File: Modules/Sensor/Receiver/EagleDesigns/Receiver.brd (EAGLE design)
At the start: 100 x 80 mm, 11 parts, among them U2 ATMEGA328P_TQFP

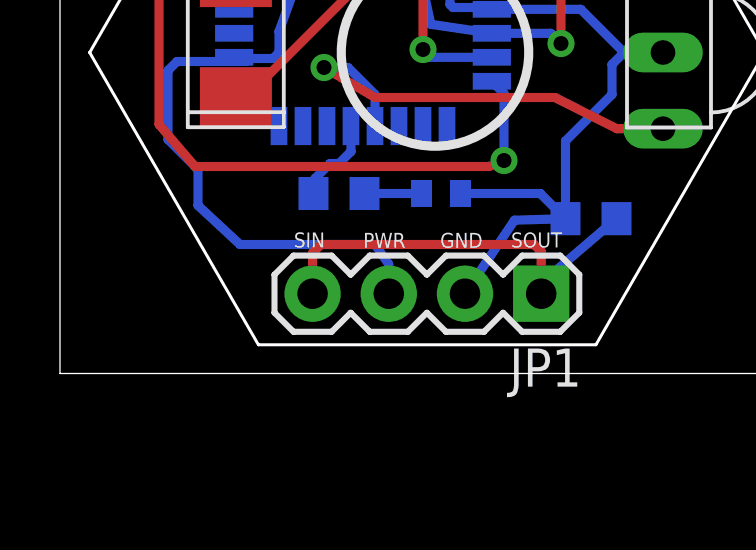
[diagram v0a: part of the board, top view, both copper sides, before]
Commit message: fixed eagle files for new modules
SIN/SOUT was not correctly connected in them.
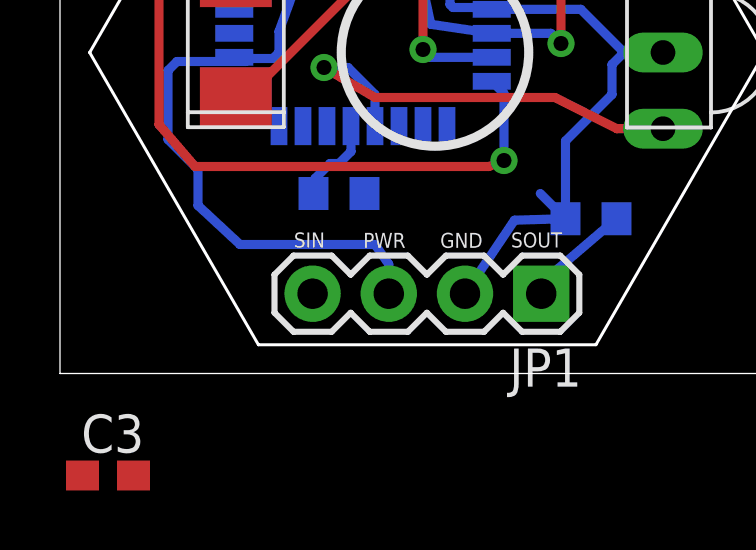
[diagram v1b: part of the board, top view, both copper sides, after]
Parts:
- C3: device adafruit:C0402 -> adafruit:C0603
- moved C3 14.5 mm to (1.60, -3.40), flipped to the top, turned to 0 degrees
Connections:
- removed net 1X3SIN-SOUT: JP1.1, JP1.4, R1.2
- net 1X3SIN: now also JP1.4, R1.2
- net 1X3SOUT: now also JP1.1
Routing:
- net 1X3SIN-SOUT: track 14.4 -> 0.00 mm
- net 1X3SIN: track 0.00 -> 3.55 mm
- net GND: track 43.7 -> 41.0 mm
- net 1X3SOUT: track 1.90 -> 0.00 mm
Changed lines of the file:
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@@
 </element>
 <element name="R4" library="adafruit" package="R0603" value="4.7K" x="9.3" y="6" rot="MR0"/>
-<element name="C3" library="adafruit" package="C0402" value="0.22uF" x="12.7" y="6" rot="MR180"/>
 <element name="U$1" library="tsop" package="TSOP382XX,384XX" value="TSOP38238" x="21.7" y="10.7" rot="R90"/>
+<element name="C3" library="adafruit" package="C0603" value="0.22uF" x="1.6" y="-3.4"/>
 </elements>
 <signals>
@@
 <wire x1="16.85" y1="5.16" x2="15.15" y2="5.11" width="0.3048" layer="16"/>
 <wire x1="15.15" y1="5.11" x2="13.5" y2="2.66" width="0.3048" layer="16"/>
-<contactref element="C3" pad="2"/>
 <contactref element="U$1" pad="GND"/>
 <wire x1="12.25" y1="16.55" x2="9.95" y2="16.55" width="0.3048" layer="1"/>
@@
 <wire x1="14.3926" y1="12.14" x2="17.36" y2="12.14" width="0.3048" layer="16"/>
 <wire x1="17.36" y1="12.14" x2="18.8" y2="10.7" width="0.3048" layer="16"/>
-<wire x1="13.35" y1="6" x2="16.01" y2="6" width="0.3048" layer="16"/>
 <wire x1="16.01" y1="6" x2="16.85" y2="5.16" width="0.3048" layer="16"/>
 <wire x1="7.89" y1="16.55" x2="9.95" y2="16.55" width="0.3048" layer="1"/>
@@
 <via x="10" y="14.7" extent="1-16" drill="0.5"/>
 <wire x1="10" y1="14.7" x2="10" y2="15.5" width="0.3048" layer="16"/>
-</signal>
-<signal name="1X3SIN-SOUT">
-<contactref element="JP1" pad="4"/>
-<contactref element="JP1" pad="1"/>
-<contactref element="R1" pad="2"/>
-<wire x1="18.55" y1="5.16" x2="15.85" y2="2.85" width="0.3048" layer="16"/>
-<wire x1="15.85" y1="2.85" x2="16.04" y2="2.66" width="0.3048" layer="16"/>
-<wire x1="16.04" y1="2.66" x2="16.04" y2="4.06" width="0.3048" layer="1"/>
-<wire x1="16.04" y1="4.06" x2="15.8" y2="4.3" width="0.3048" layer="1"/>
-<wire x1="8.42" y1="2.66" x2="8.42" y2="4.02" width="0.3048" layer="1"/>
-<wire x1="8.42" y1="4.02" x2="8.7" y2="4.3" width="0.3048" layer="1"/>
-<wire x1="8.7" y1="4.3" x2="15.8" y2="4.3" width="0.3048" layer="1"/>
+<contactref element="C3" pad="2"/>
+<wire x1="2.45" y1="-3.4" x2="13.5" y2="2.66" width="0" layer="19" extent="1-1"/>
 </signal>
 <signal name="RESET">
@@
 <signal name="1X3SIN">
 <contactref element="U2" pad="23"/>
+<contactref element="JP1" pad="4"/>
+<contactref element="R1" pad="2"/>
+<wire x1="18.55" y1="5.16" x2="15.85" y2="2.85" width="0.3048" layer="16"/>
+<wire x1="8.42" y1="2.66" x2="5.8074" y2="14.54" width="0" layer="19" extent="16-16"/>
+<wire x1="15.85" y1="2.85" x2="8.42" y2="2.66" width="0" layer="19" extent="16-16"/>
 </signal>
 <signal name="N$1">
@@
 <contactref element="R4" pad="1"/>
 <contactref element="C3" pad="1"/>
-<wire x1="10.15" y1="6" x2="12.05" y2="6" width="0.3048" layer="16"/>
+<contactref element="JP1" pad="1"/>
+<wire x1="10.15" y1="6" x2="16.04" y2="2.66" width="0" layer="19" extent="16-16"/>
+<wire x1="0.75" y1="-3.4" x2="10.15" y2="6" width="0" layer="19" extent="1-16"/>
 </signal>
 <signal name="OUT">

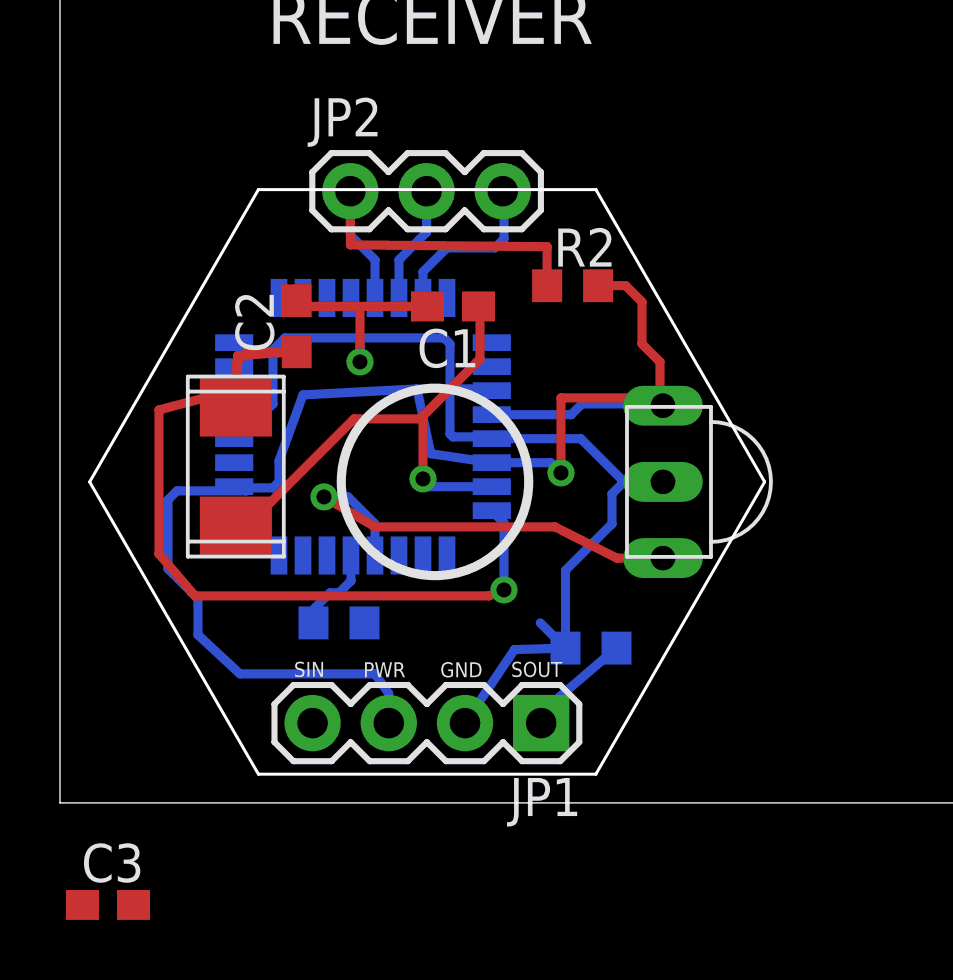
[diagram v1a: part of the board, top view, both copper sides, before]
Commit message: Receiver: added final PCB #29
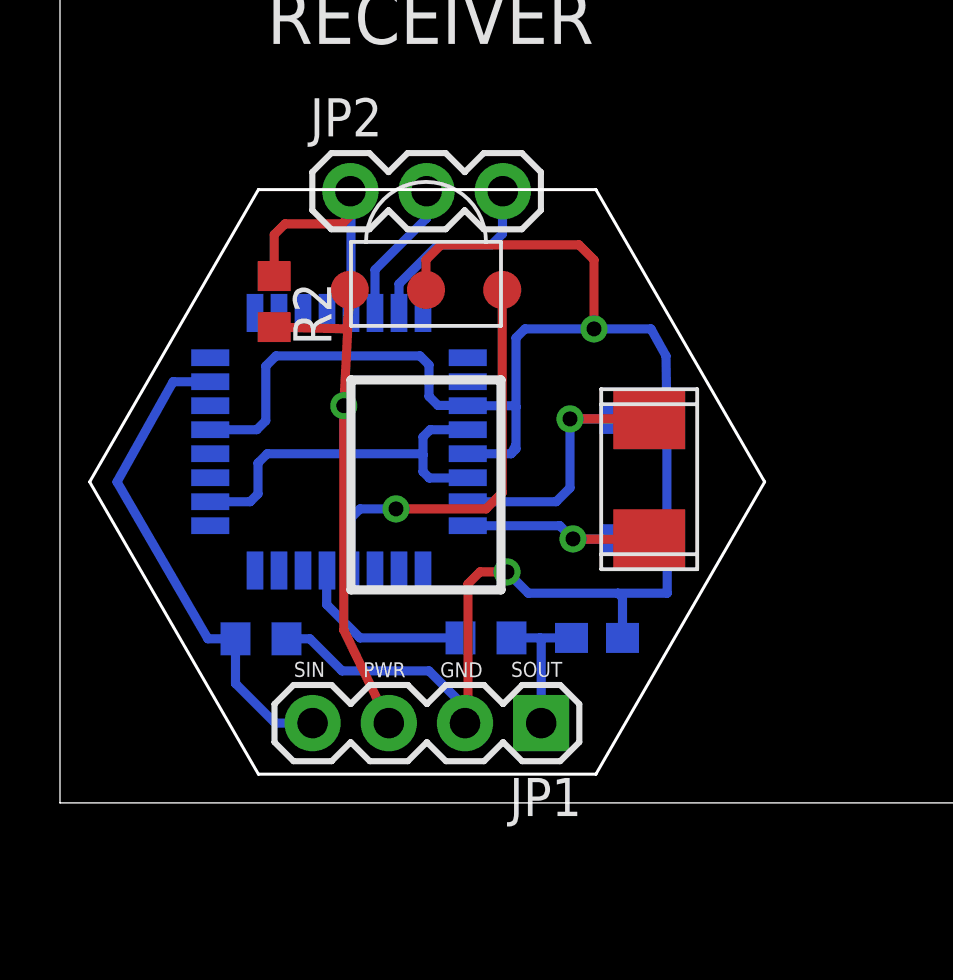
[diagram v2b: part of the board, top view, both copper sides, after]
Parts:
- U$1: value TSOP38238 -> IR-RECEIVER; device tsop:TSOP382XX,384XX -> MakerWear:TSOP382XX,384XX
- moved C3 18.6 mm to (17.9, 5.50), flipped to the bottom, turned to 180 degrees
- moved U$2 13.8 mm to (19.6, 10.8), turned to 270 degrees
- moved C2 13.5 mm to (19.4, 8.79), flipped to the bottom, turned to 180 degrees
- moved U$1 12.4 mm to (12.2, 18.7), turned to 180 degrees
- moved R1 11.0 mm to (6.70, 5.47), turned to 0 degrees
- moved R2 9.96 mm to (7.14, 16.7), turned to 270 degrees
- moved C1 7.31 mm to (19.4, 12.8), flipped to the bottom
- moved R4 4.93 mm to (14.2, 5.50)
- moved U2 0.94 mm to (9.30, 12.0)
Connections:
- net VCC: now also U$1.VSS; no longer U$1.VS
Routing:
- net GND: track 41.0 -> 62.9 mm, vias 1 -> 2
- net N$3: track 29.2 -> 7.68 mm
- net VCC: track 48.4 -> 32.9 mm
- net 1X3SIN: track 3.55 -> 16.6 mm
- net N$1: track 17.7 -> 10.1 mm
- net 1X3SOUT: track 0.00 -> 4.86 mm
- net RESET: track 13.5 -> 9.08 mm
- net OUT: track 2.94 -> 6.06 mm
- net IR-IN: track 14.9 -> 13.9 mm
- net TX: track 5.62 -> 6.53 mm
- net RX: track 3.94 -> 4.77 mm

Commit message: minor organizations
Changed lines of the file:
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@@
 <wire x1="9.5" y1="11.64" x2="12.06" y2="11.64" width="0.3048" layer="16"/>
 <wire x1="12.06" y1="11.64" x2="12.1" y2="11.6" width="0.3048" layer="16"/>
-<wire x1="9.66" y1="17.1" x2="9.46" y2="13.24" width="0.3048" layer="1"/>
-<via x="9.46" y="13.24" extent="1-16" drill="0.5"/>
-<wire x1="10.96" y1="2.66" x2="9.46" y2="5.76" width="0.3048" layer="1"/>
-<wire x1="9.46" y1="5.76" x2="9.46" y2="13.24" width="0.3048" layer="1"/>
-<wire x1="9.46" y1="13.24" x2="9.46" y2="11.68" width="0.3048" layer="16"/>
-<wire x1="9.46" y1="11.68" x2="9.5" y2="11.64" width="0.3048" layer="16"/>
-<wire x1="9.66" y1="17.1" x2="9.58" y2="15.8" width="0.3048" layer="1"/>
-<wire x1="9.58" y1="15.8" x2="7.14" y2="15.86" width="0.3048" layer="1"/>
+<via x="9.66" y="13.24" extent="1-16" drill="0.5"/>
+<wire x1="9.66" y1="13.24" x2="9.66" y2="11.68" width="0.3048" layer="16"/>
+<wire x1="9.66" y1="11.68" x2="9.5" y2="11.64" width="0.3048" layer="16"/>
+<wire x1="7.14" y1="15.86" x2="9.66" y2="15.86" width="0.3048" layer="1"/>
+<wire x1="9.66" y1="15.86" x2="9.66" y2="17.1" width="0.3048" layer="1"/>
+<wire x1="9.66" y1="15.86" x2="9.66" y2="13.24" width="0.3048" layer="1"/>
+<wire x1="9.66" y1="5.34" x2="9.66" y2="13.24" width="0.3048" layer="1"/>
+<wire x1="10.96" y1="2.66" x2="10.96" y2="4.84" width="0.3048" layer="1"/>
+<wire x1="10.96" y1="4.84" x2="10.7" y2="5.1" width="0.3048" layer="1"/>
+<wire x1="9.66" y1="5.34" x2="9.9" y2="5.1" width="0.3048" layer="1"/>
+<wire x1="9.9" y1="5.1" x2="10.7" y2="5.1" width="0.3048" layer="1"/>
 </signal>
 <signal name="GND">

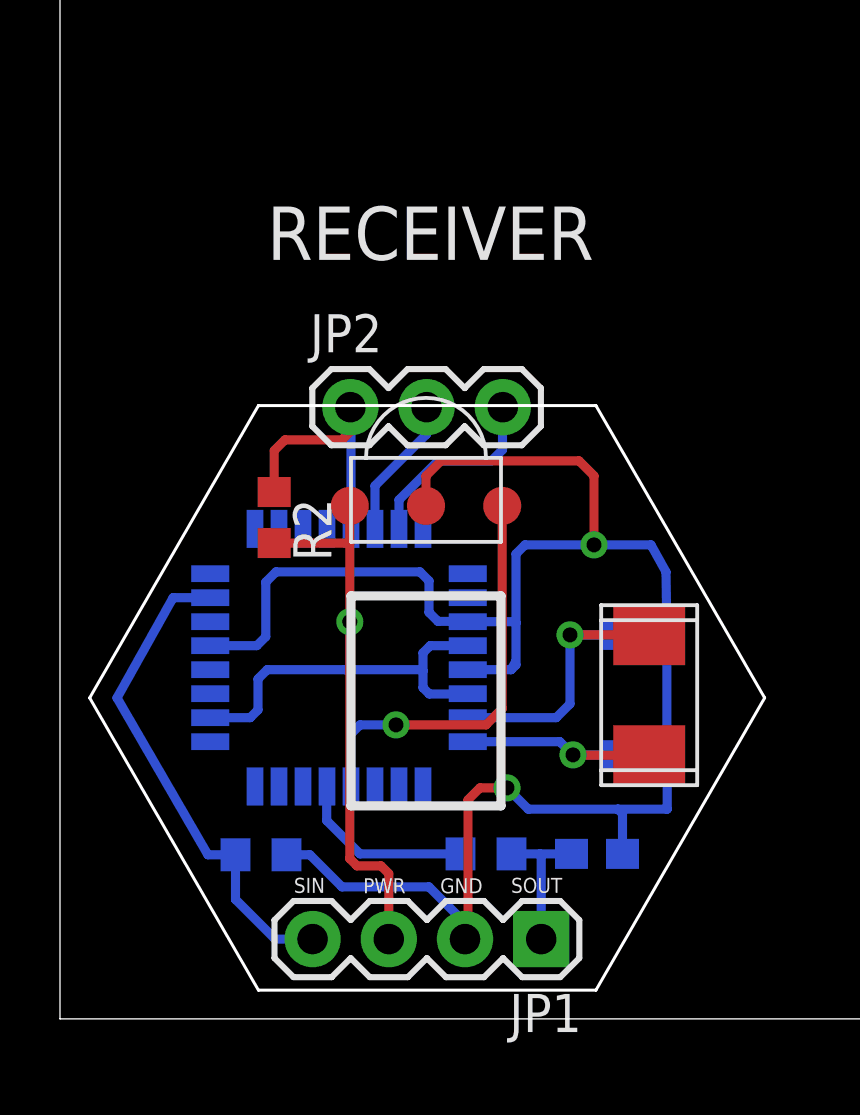
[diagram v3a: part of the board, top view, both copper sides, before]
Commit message: added version numbers, and deleted most of the text that was on each module.
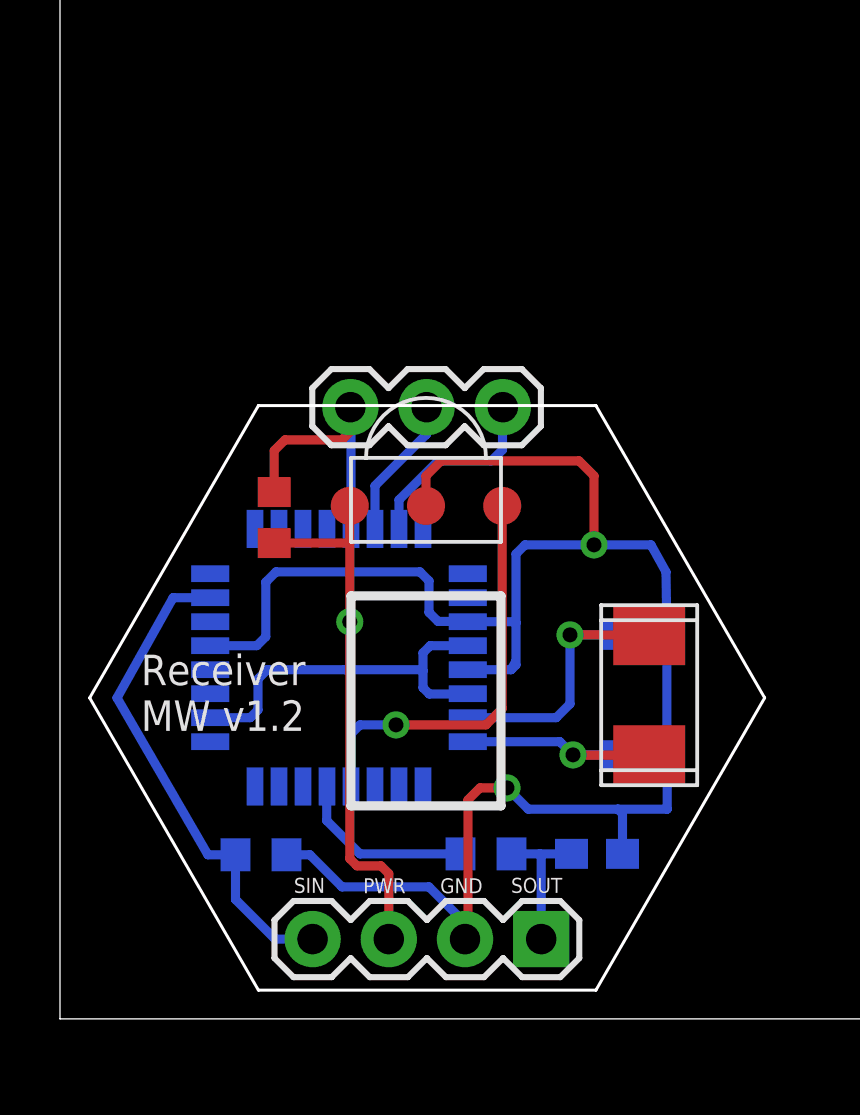
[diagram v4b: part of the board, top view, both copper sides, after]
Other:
- board text added: "Receiver MW v1.2"
- board text removed: "RECEIVER"
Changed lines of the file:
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@@
 <layer number="19" name="Unrouted" color="6" fill="1" visible="yes" active="yes"/>
 <layer number="20" name="Dimension" color="15" fill="1" visible="yes" active="yes"/>
-<layer number="21" name="tPlace" color="7" fill="1" visible="no" active="yes"/>
-<layer number="22" name="bPlace" color="7" fill="1" visible="no" active="yes"/>
-<layer number="23" name="tOrigins" color="15" fill="1" visible="no" active="yes"/>
-<layer number="24" name="bOrigins" color="15" fill="1" visible="no" active="yes"/>
-<layer number="25" name="tNames" color="7" fill="1" visible="no" active="yes"/>
-<layer number="26" name="bNames" color="7" fill="1" visible="no" active="yes"/>
-<layer number="27" name="tValues" color="7" fill="1" visible="no" active="yes"/>
-<layer number="28" name="bValues" color="7" fill="1" visible="no" active="yes"/>
+<layer number="21" name="tPlace" color="7" fill="1" visible="yes" active="yes"/>
+<layer number="22" name="bPlace" color="7" fill="1" visible="yes" active="yes"/>
+<layer number="23" name="tOrigins" color="15" fill="1" visible="yes" active="yes"/>
+<layer number="24" name="bOrigins" color="15" fill="1" visible="yes" active="yes"/>
+<layer number="25" name="tNames" color="7" fill="1" visible="yes" active="yes"/>
+<layer number="26" name="bNames" color="7" fill="1" visible="yes" active="yes"/>
+<layer number="27" name="tValues" color="7" fill="1" visible="yes" active="yes"/>
+<layer number="28" name="bValues" color="7" fill="1" visible="yes" active="yes"/>
 <layer number="29" name="tStop" color="7" fill="3" visible="no" active="yes"/>
 <layer number="30" name="bStop" color="7" fill="6" visible="no" active="yes"/>
@@
 <text x="12.6723" y="4.188" size="0.5" layer="21">GND</text>
 <text x="15.0345" y="4.2007" size="0.5" layer="21">SOUT</text>
-<text x="6.9" y="25.3" size="1.778" layer="21">RECEIVER</text>
 <wire x1="9.7" y1="14.1" x2="14.7" y2="14.1" width="0.3048" layer="21"/>
 <wire x1="14.7" y1="14.1" x2="14.7" y2="7.1" width="0.3048" layer="21"/>
 <wire x1="14.7" y1="7.1" x2="9.7" y2="7.1" width="0.3048" layer="21"/>
 <wire x1="9.7" y1="7.1" x2="9.7" y2="14.1" width="0.3048" layer="21"/>
+<text x="2.7" y="9.6" size="1.016" layer="21">Receiver
+MW v1.2</text>
 </plain>
 <attributes>
@@
 </autorouter>
 <elements>
-<element name="C1" library="adafruit" package="C0603" value="22pF" x="19.38" y="12.8" rot="MR180"/>
-<element name="C2" library="adafruit" package="C0603" value="22pF" x="19.39" y="8.79" rot="MR180"/>
-<element name="JP1" library="SparkFun-Connectors" package="1X04" value="" x="16.04" y="2.66" rot="R180"/>
-<element name="JP2" library="SparkFun-Connectors" package="1X03" value="" x="9.68" y="20.39"/>
-<element name="R1" library="adafruit" package="R0603" value="1M" x="6.7" y="5.47" rot="MR0"/>
-<element name="R2" library="resistor" package="R0603" value="10K" x="7.14" y="16.71" rot="R270"/>
-<element name="U$2" library="MakerWear" package="NX503" value="NX503" x="19.64" y="10.79" rot="R270"/>
-<element name="U2" library="SparkFun-DigitalIC" package="TQFP32-08" value="ATMEGA328P_TQFP" x="9.3" y="12.04" rot="MR0">
+<element name="C1" library="adafruit" package="C0603" value="22pF" x="19.38" y="12.8" smashed="yes" rot="MR180"/>
+<element name="C2" library="adafruit" package="C0603" value="22pF" x="19.39" y="8.79" smashed="yes" rot="MR180"/>
+<element name="JP1" library="SparkFun-Connectors" package="1X04" value="" x="16.04" y="2.66" smashed="yes" rot="R180">
+<attribute name="VALUE" x="17.31" y="5.835" size="1.27" layer="27" rot="R180"/>
+</element>
+<element name="JP2" library="SparkFun-Connectors" package="1X03" value="" x="9.68" y="20.39" smashed="yes">
+<attribute name="VALUE" x="8.41" y="17.215" size="1.27" layer="27"/>
+</element>
+<element name="R1" library="adafruit" package="R0603" value="1M" x="6.7" y="5.47" smashed="yes" rot="MR0"/>
+<element name="R2" library="resistor" package="R0603" value="10K" x="7.14" y="16.71" smashed="yes" rot="R270"/>
+<element name="U$2" library="MakerWear" package="NX503" value="NX503" x="19.64" y="10.79" smashed="yes" rot="R270"/>
+<element name="U2" library="SparkFun-DigitalIC" package="TQFP32-08" value="ATMEGA328P_TQFP" x="9.3" y="12.04" smashed="yes" rot="MR0">
 <attribute name="PROD_ID" value="IC-09069" x="9.3" y="12.04" size="1.778" layer="28" rot="MR0" display="off"/>
 </element>
-<element name="R4" library="adafruit" package="R0603" value="4.7K" x="14.2" y="5.5" rot="MR0"/>
-<element name="C3" library="adafruit" package="C0603" value="0.22uF" x="17.9" y="5.5" rot="MR180"/>
-<element name="U$1" library="MakerWear" package="TSOP382XX,384XX" value="IR-RECEIVER" x="12.2" y="18.7" rot="R180"/>
+<element name="R4" library="adafruit" package="R0603" value="4.7K" x="14.2" y="5.5" smashed="yes" rot="MR0"/>
+<element name="C3" library="adafruit" package="C0603" value="0.22uF" x="17.9" y="5.5" smashed="yes" rot="MR180"/>
+<element name="U$1" library="MakerWear" package="TSOP382XX,384XX" value="IR-RECEIVER" x="12.2" y="18.7" smashed="yes" rot="R180"/>
 </elements>
 <signals>
@@
 </board>
 </drawing>
+<compatibility>
+<note version="6.3" minversion="6.2.2" severity="warning">
+Since Version 6.2.2 text objects can contain more than one line,
+which will not be processed correctly with this version.
+</note>
+</compatibility>
 </eagle>
